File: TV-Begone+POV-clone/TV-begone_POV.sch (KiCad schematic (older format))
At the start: 38 parts, among them J1 CONN_3, Q1 BC547, Q2 BC547, Q3 BC547, Q4 BC547, Q5 BC557, SW1 SW_PUSH, SW2 CONN_2X2, U1 ATTINY24-44-84/DIP-SO, X1 8MHz

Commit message: tilføjet footprints til det hele, og startet på layout.. -ish...
git-svn-id: file:///home/ff/projects/osaa/svn@154 a092026d-3e22-4cff-94a7-eaa6fdd35d37
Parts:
- gave numbers to parts that had none: 2
- renumbered BATT+ to BATT+1, BATT- to BATT-1, PROG to PROG1
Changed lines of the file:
@@
-EESchema Schematic File Version 2  date 19-10-2010 20:40:57
+EESchema Schematic File Version 2  date 26-10-2010 19:43:10
 LIBS:power
 LIBS:device
@@
 Sheet 1 1
 Title ""
-Date "19 oct 2010"
+Date "26 oct 2010"
 Rev ""
 Comp ""
@@
 Connection ~ 4125 3625
 $Comp
-L VCC #PWR?
+L VCC #PWR01
 U 1 1 4CBDE3DA
 P 4625 3375
-F 0 "#PWR?" H 4625 3475 30  0001 C CNN
+F 0 "#PWR01" H 4625 3475 30  0001 C CNN
 F 1 "VCC" H 4625 3475 30  0000 C CNN
 	1    4625 3375
@@
 $EndComp
 $Comp
-L R R?
+L R R10
 U 1 1 4CBDE3D1
 P 4375 3500
-F 0 "R?" V 4455 3500 50  0000 C CNN
+F 0 "R10" V 4455 3500 50  0000 C CNN
 F 1 "1K" V 4375 3500 50  0000 C CNN
 	1    4375 3500
@@
 $EndComp
 $Comp
-L GND #PWR?
+L GND #PWR02
 U 1 1 4CBC19E2
 P 9825 4350
-F 0 "#PWR?" H 9825 4350 30  0001 C CNN
+F 0 "#PWR02" H 9825 4350 30  0001 C CNN
 F 1 "GND" H 9825 4280 30  0001 C CNN
 	1    9825 4350
@@
 $EndComp
 $Comp
-L VCC #PWR?
+L VCC #PWR03
 U 1 1 4CBC19DA
 P 8725 3375
-F 0 "#PWR?" H 8725 3475 30  0001 C CNN
+F 0 "#PWR03" H 8725 3475 30  0001 C CNN
 F 1 "VCC" H 8725 3475 30  0000 C CNN
 	1    8725 3375
@@
 $EndComp
 $Comp
-L CP1 C?
+L CP1 C3
 U 1 1 4CBC19C3
 P 9200 4025
-F 0 "C?" H 9250 4125 50  0000 L CNN
+F 0 "C3" H 9250 4125 50  0000 L CNN
 F 1 "10n" H 9250 3925 50  0000 L CNN
 	1    9200 4025
@@
 TV Begone IR LEDs
 $Comp
-L VCC #PWR?
+L VCC #PWR04
 U 1 1 4CBC146A
 P 6375 4050
-F 0 "#PWR?" H 6375 4150 30  0001 C CNN
+F 0 "#PWR04" H 6375 4150 30  0001 C CNN
 F 1 "VCC" H 6375 4150 30  0000 C CNN
 	1    6375 4050
@@
 $EndComp
 $Comp
-L VCC #PWR?
+L VCC #PWR05
 U 1 1 4CBC12ED
 P 7750 4350
-F 0 "#PWR?" H 7750 4450 30  0001 C CNN
+F 0 "#PWR05" H 7750 4450 30  0001 C CNN
 F 1 "VCC" H 7750 4450 30  0000 C CNN
 	1    7750 4350
@@
 $EndComp
 $Comp
-L GND #PWR?
+L GND #PWR06
 U 1 1 4CBC12B5
 P 7150 6900
-F 0 "#PWR?" H 7150 6900 30  0001 C CNN
+F 0 "#PWR06" H 7150 6900 30  0001 C CNN
 F 1 "GND" H 7150 6830 30  0001 C CNN
 	1    7150 6900
@@
 MISO
 $Comp
-L GND #PWR01
+L GND #PWR07
 U 1 1 4CBC0E53
 P 5575 3500
-F 0 "#PWR01" H 5575 3500 30  0001 C CNN
+F 0 "#PWR07" H 5575 3500 30  0001 C CNN
 F 1 "GND" H 5575 3430 30  0001 C CNN
 	1    5575 3500
@@
 $EndComp
 $Comp
-L VCC #PWR02
+L VCC #PWR08
 U 1 1 4CBC0DDF
 P 900 975
-F 0 "#PWR02" H 900 1075 30  0001 C CNN
+F 0 "#PWR08" H 900 1075 30  0001 C CNN
 F 1 "VCC" H 900 1075 30  0000 C CNN
 	1    900  975
@@
 $EndComp
 $Comp
-L GND #PWR03
+L GND #PWR09
 U 1 1 4CBC0DDA
 P 900 1225
-F 0 "#PWR03" H 900 1225 30  0001 C CNN
+F 0 "#PWR09" H 900 1225 30  0001 C CNN
 F 1 "GND" H 900 1155 30  0001 C CNN
 	1    900  1225
@@
 $EndComp
 $Comp
-L CONN_1 BATT-
+L CONN_1 BATT-1
 U 1 1 4CBC0DB5
 P 675 1325
-F 0 "BATT-" H 755 1325 40  0000 L CNN
+F 0 "BATT-1" H 755 1325 40  0000 L CNN
 F 1 "CONN_1" H 675 1380 30  0001 C CNN
 	1    675  1325
@@
 $EndComp
 $Comp
-L CONN_1 BATT+
+L CONN_1 BATT+1
 U 1 1 4CBC0DAF
 P 675 900
-F 0 "BATT+" H 755 900 40  0000 L CNN
+F 0 "BATT+1" H 755 900 40  0000 L CNN
 F 1 "CONN_1" H 675 955 30  0001 C CNN
 	1    675  900
@@
 $EndComp
 $Comp
-L GND #PWR04
+L GND #PWR010
 U 1 1 4CBC0D36
 P 2925 6450
-F 0 "#PWR04" H 2925 6450 30  0001 C CNN
+F 0 "#PWR010" H 2925 6450 30  0001 C CNN
 F 1 "GND" H 2925 6380 30  0001 C CNN
 	1    2925 6450
@@
 $EndComp
 $Comp
-L VCC #PWR05
+L VCC #PWR011
 U 1 1 4CBC0D30
 P 2925 6025
-F 0 "#PWR05" H 2925 6125 30  0001 C CNN
+F 0 "#PWR011" H 2925 6125 30  0001 C CNN
 F 1 "VCC" H 2925 6125 30  0000 C CNN
 	1    2925 6025
@@
 $EndComp
 $Comp
-L CONN_3X2 PROG
+L CONN_3X2 PROG1
 U 1 1 4CBC0D13
 P 2400 6275
-F 0 "PROG" H 2400 6525 50  0000 C CNN
+F 0 "PROG1" H 2400 6525 50  0000 C CNN
 F 1 "CONN_3X2" V 2400 6325 40  0000 C CNN
 	1    2400 6275
@@
 $EndComp
 $Comp
-L VCC #PWR06
+L VCC #PWR012
 U 1 1 4CBC0BB2
 P 7450 825
-F 0 "#PWR06" H 7450 925 30  0001 C CNN
+F 0 "#PWR012" H 7450 925 30  0001 C CNN
 F 1 "VCC" H 7450 925 30  0000 C CNN
 	1    7450 825
@@
 $EndComp
 $Comp
-L GND #PWR07
+L GND #PWR013
 U 1 1 4CBC08BA
 P 1700 4000
-F 0 "#PWR07" H 1700 4000 30  0001 C CNN
+F 0 "#PWR013" H 1700 4000 30  0001 C CNN
 F 1 "GND" H 1700 3930 30  0001 C CNN
 	1    1700 4000
@@
 $EndComp
 $Comp
-L GND #PWR08
+L GND #PWR014
 U 1 1 4CBC0821
 P 1350 1425
-F 0 "#PWR08" H 1350 1425 30  0001 C CNN
+F 0 "#PWR014" H 1350 1425 30  0001 C CNN
 F 1 "GND" H 1350 1355 30  0001 C CNN
 	1    1350 1425
@@
 $EndComp
 $Comp
-L VCC #PWR09
+L VCC #PWR015
 U 1 1 4CBC0819
 P 1350 775
-F 0 "#PWR09" H 1350 875 30  0001 C CNN
+F 0 "#PWR015" H 1350 875 30  0001 C CNN
 F 1 "VCC" H 1350 875 30  0000 C CNN
 	1    1350 775
@@
 $EndComp
 $Comp
-L VCC #PWR010
+L VCC #PWR016
 U 1 1 4CBC0760
 P 1100 1775
-F 0 "#PWR010" H 1100 1875 30  0001 C CNN
+F 0 "#PWR016" H 1100 1875 30  0001 C CNN
 F 1 "VCC" H 1100 1875 30  0000 C CNN
 	1    1100 1775
@@
 $EndComp
 $Comp
-L GND #PWR011
+L GND #PWR017
 U 1 1 4CBC06BE
 P 1100 2200
-F 0 "#PWR011" H 1100 2200 30  0001 C CNN
+F 0 "#PWR017" H 1100 2200 30  0001 C CNN
 F 1 "GND" H 1100 2130 30  0001 C CNN
 	1    1100 2200

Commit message: added footprints to the lot of them.. (batt hullerne er stadig forkerte) er begyndt på board layout
git-svn-id: file:///home/ff/projects/osaa/svn@157 a092026d-3e22-4cff-94a7-eaa6fdd35d37
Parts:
- removed SW2: CONN_2X2, symbol CONN_2X2
- added J2: CONN_4X2, symbol CONN_4X2
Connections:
- wire segments 112 -> 114
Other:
- moved on the sheet: C3

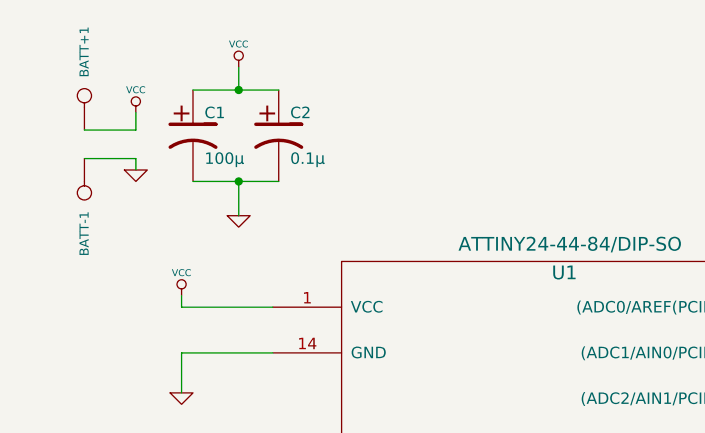
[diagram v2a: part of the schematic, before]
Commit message: changed C2 to ceramic cap, started routing board
git-svn-id: file:///home/ff/projects/osaa/svn@158 a092026d-3e22-4cff-94a7-eaa6fdd35d37
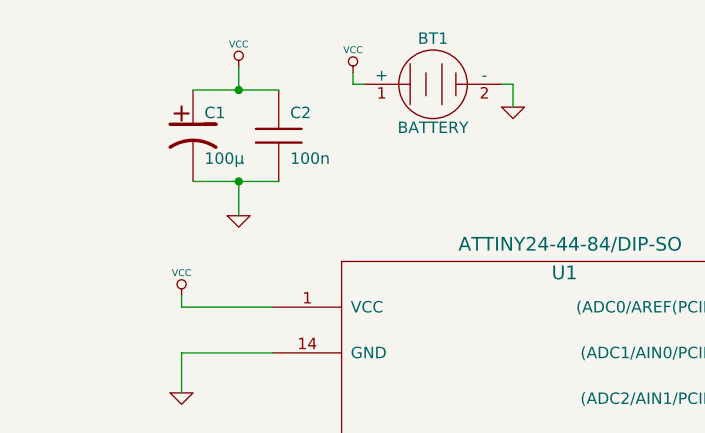
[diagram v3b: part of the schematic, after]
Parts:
- removed BATT+1, BATT-1: CONN_1, symbol CONN_1
- removed C2: 0.1µ, symbol CP1
- added BT1: BATTERY, symbol BATTERY
- added C2: 100n, symbol C
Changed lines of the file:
@@
-EESchema Schematic File Version 2  date 27-10-2010 21:50:11
+EESchema Schematic File Version 2  date 28-10-2010 10:43:23
 LIBS:power
 LIBS:device
@@
 Sheet 1 1
 Title ""
-Date "27 oct 2010"
+Date "28 oct 2010"
 Rev ""
 Comp ""
@@
 $EndDescr
 Wire Wire Line
+	2550 950  2550 850
+Wire Wire Line
+	2550 850  2500 850
+Wire Wire Line
 	1500 4425 1425 4425
 Wire Wire Line
@@
 	7150 5000 6900 5000
 Wire Wire Line
-	900  975  900  1050
-Wire Wire Line
-	900  1225 900  1175
-Wire Wire Line
-	900  1175 675  1175
-Wire Wire Line
 	2000 6325 1725 6325
 Wire Wire Line
@@
 Wire Wire Line
 	1700 6125 2000 6125
-Wire Wire Line
-	900  1050 675  1050
 Wire Wire Line
 	7150 6800 6900 6800
@@
 Wire Wire Line
 	1500 3800 1425 3800
+Wire Wire Line
+	1900 850  1850 850
+Wire Wire Line
+	1850 850  1850 800
+$Comp
+L GND #PWR?
+U 1 1 4CC93783
+P 2550 950
+F 0 "#PWR?" H 2550 950 30  0001 C CNN
+F 1 "GND" H 2550 880 30  0001 C CNN
+	1    2550 950
+	1    0    0    -1
+$EndComp
+$Comp
+L VCC #PWR?
+U 1 1 4CC9377A
+P 1850 800
+F 0 "#PWR?" H 1850 900 30  0001 C CNN
+F 1 "VCC" H 1850 900 30  0000 C CNN
+	1    1850 800
+	1    0    0    -1
+$EndComp
+$Comp
+L BATTERY BT1
+U 1 1 4CC9376A
+P 2200 850
+F 0 "BT1" H 2200 1050 50  0000 C CNN
+F 1 "BATTERY" H 2200 660 50  0000 C CNN
+	1    2200 850
+	1    0    0    -1
+$EndComp
+$Comp
+L C C2
+U 1 1 4CC935ED
+P 1525 1075
+F 0 "C2" H 1575 1175 50  0000 L CNN
+F 1 "100n" H 1575 975 50  0000 L CNN
+	1    1525 1075
+	1    0    0    -1
+$EndComp
 $Comp
 L CONN_4X2 J2
@@
 $EndComp
 $Comp
-L VCC #PWR08
-U 1 1 4CBC0DDF
-P 900 975
-F 0 "#PWR08" H 900 1075 30  0001 C CNN
-F 1 "VCC" H 900 1075 30  0000 C CNN
-	1    900  975
-	1    0    0    -1
-$EndComp
-$Comp
-L GND #PWR09
-U 1 1 4CBC0DDA
-P 900 1225
-F 0 "#PWR09" H 900 1225 30  0001 C CNN
-F 1 "GND" H 900 1155 30  0001 C CNN
-	1    900  1225
-	1    0    0    -1
-$EndComp
-$Comp
-L CONN_1 BATT-1
-U 1 1 4CBC0DB5
-P 675 1325
-F 0 "BATT-1" H 755 1325 40  0000 L CNN
-F 1 "CONN_1" H 675 1380 30  0001 C CNN
-	1    675  1325
-	0    1    1    0
-$EndComp
-$Comp
-L CONN_1 BATT+1
-U 1 1 4CBC0DAF
-P 675 900
-F 0 "BATT+1" H 755 900 40  0000 L CNN
-F 1 "CONN_1" H 675 955 30  0001 C CNN
-	1    675  900
-	0    -1   -1   0
-$EndComp
-$Comp
 L GND #PWR010
 U 1 1 4CBC0D36
@@
 	1    0    0    -1
 $EndComp
-$Comp
-L CP1 C2
-U 1 1 4CBC07E4
-P 1525 1075
-F 0 "C2" H 1575 1175 50  0000 L CNN
-F 1 "0.1µ" H 1575 975 50  0000 L CNN
-	1    1525 1075
-	1    0    0    -1
-$EndComp
